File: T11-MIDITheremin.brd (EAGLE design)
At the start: 101.6 x 76.2 mm, 102 parts, among them IC1 TL072P, IC2 TL072P, T1 2N3904, T2 2N3904, T3 2N3904, T4 2N3904, T5 2N3904

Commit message: Add files via upload
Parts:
- removed L4, L5, L6: 10mH, rcl:6000-XXXX-RC
- added C32: 2200pF, resistor:C050-025X075
- C2, C4: value 3n3 .1% -> 1.2nF
- L1: value 100uH .1% -> 2.5mH; device rcl:6000-XXXX-RC -> resistor:0207/5V
- L2: value 100uH .1% -> 100uH; device rcl:6000-XXXX-RC -> resistor:0207/5V
- L3: value 10mH -> 100uH; device rcl:6000-XXXX-RC -> resistor:0207/5V
- moved ANT1 29.0 mm to (21.6, 58.7)
- moved L3 24.6 mm to (33.3, 52.1), turned to 90 degrees
- moved L1 20.8 mm to (14.9, 58.7), turned to 180 degrees
- moved C21 4.46 mm to (11.1, 26.7)
- moved L2 4.02 mm to (78.1, 52.1)
- moved C16 3.82 mm to (27.6, 43.8)
- moved C17 3.82 mm to (27.6, 38.7)
- moved C19 3.82 mm to (56.2, 36.2)
- moved C28 3.82 mm to (65.7, 52.1)
- moved C29 3.82 mm to (62.5, 52.1)
- moved C30 3.82 mm to (21.9, 52.1)
- moved C6 3.82 mm to (33.3, 40.6)
- moved LM2917_8 3.82 mm to (17.5, 12.7)
- moved R10 3.82 mm to (33.3, 34.3)
- moved R13 3.82 mm to (39.7, 34.3)
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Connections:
- removed net ANT: ANT1.1, L6.2
- removed net N$19: L5.1, L6.1
- removed net N$35: L4.2, L5.2
- net N$20: now also C32.1
- net N$28: now also ANT1.1, L1.1; no longer L3.1, L4.1
- net P_OSC_V+: now also L3.1; no longer L1.1
- net V-: now also C32.2
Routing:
- net ANT: track 46.4 -> 0.00 mm, vias 1 -> 0
- net GND: track 294.9 -> 262.1 mm, vias 10 -> 196
- net N$42: track 17.6 -> 0.00 mm
- net N$44: track 17.6 -> 0.00 mm
- net N$43: track 17.6 -> 0.00 mm
- net N$38: track 12.1 -> 0.00 mm
- net N$45: track 9.57 -> 0.00 mm
- net N$35: track 8.25 -> 0.00 mm
- net N$19: track 8.25 -> 0.00 mm
- net N$41: track 5.61 -> 0.00 mm
- net LOCAL_RESONANCE: track 125.1 -> 120.0 mm
- net N$28: track 8.26 -> 4.13 mm
- net N$33: track 31.6 -> 27.9 mm
- net N$20: track 7.51 -> 9.67 mm
- net V-: track 233.8 -> 235.7 mm
- added copper zone on layer 1, net GND
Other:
- board size 101.6 x 76.2 mm -> 101.6 x 62.2 mm
- board text added: "TEAM 11 11/16/16 Version 2.1"
- board text removed: "Proximity Sensor V1.0"

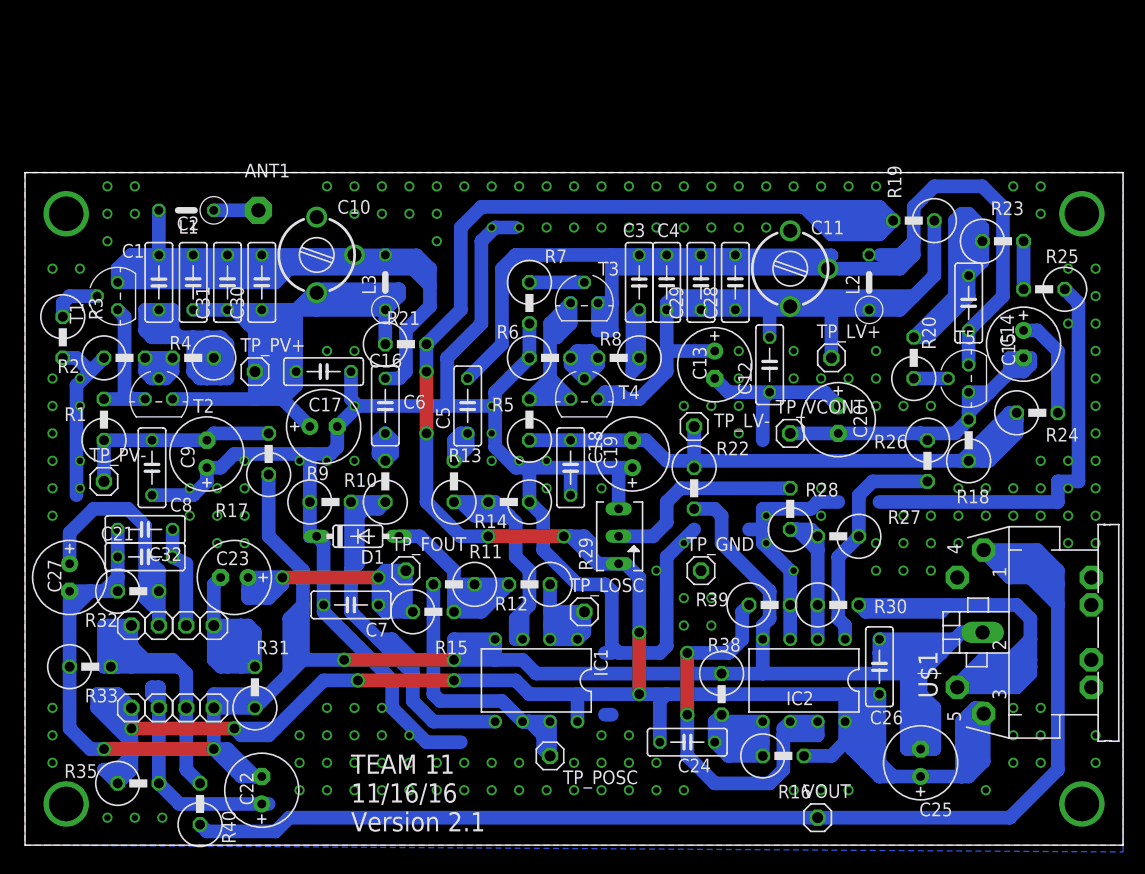
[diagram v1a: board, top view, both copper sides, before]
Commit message: fixed some of the silkscreen layer
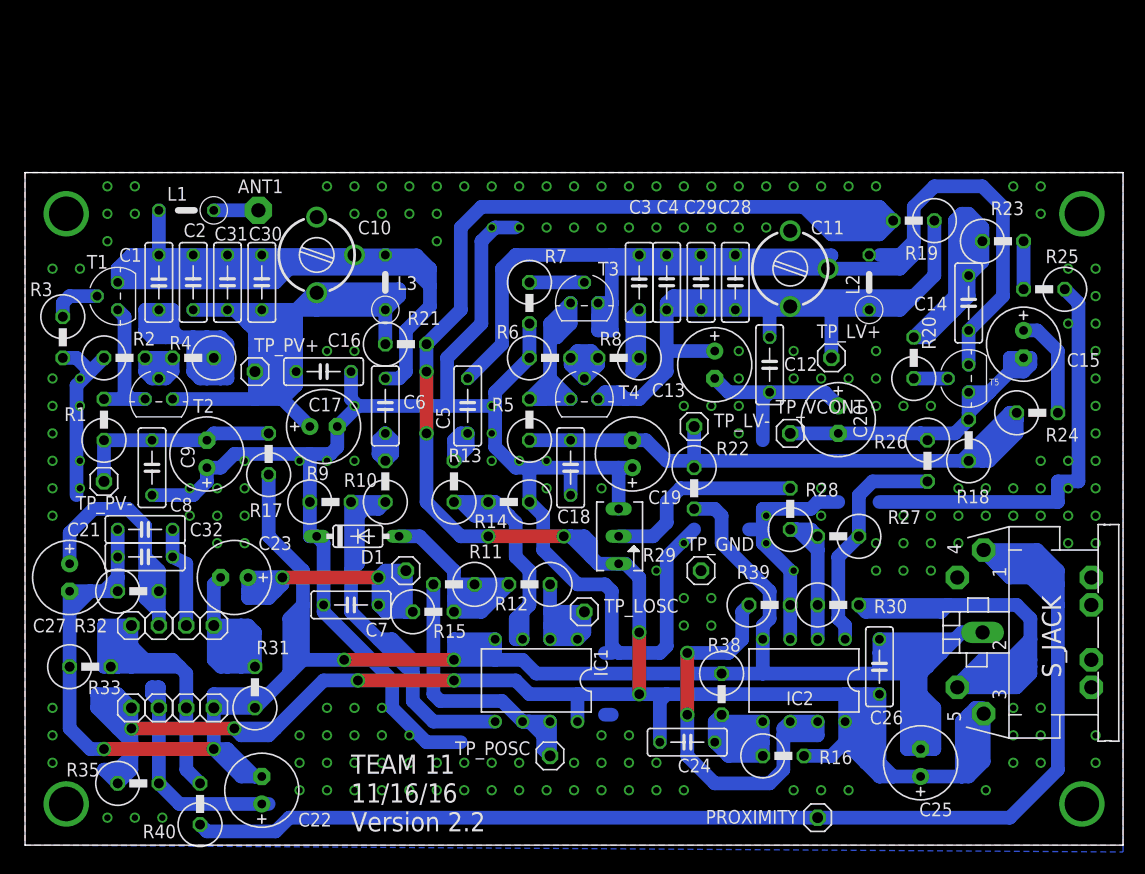
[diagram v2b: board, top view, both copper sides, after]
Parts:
- C21, C32: value 2200pF -> 3900pF
- renumbered U$1 to S_JACK, VOUT to PROXIMITY
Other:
- board text added: "TEAM 11 11/16/16 Version 2.2"
- board text removed: "TEAM 11 11/16/16 Version 2.1"
